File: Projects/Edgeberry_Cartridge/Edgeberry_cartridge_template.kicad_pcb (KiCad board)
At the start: 2 copper layers, 49.8 x 63.2 mm, 2 parts

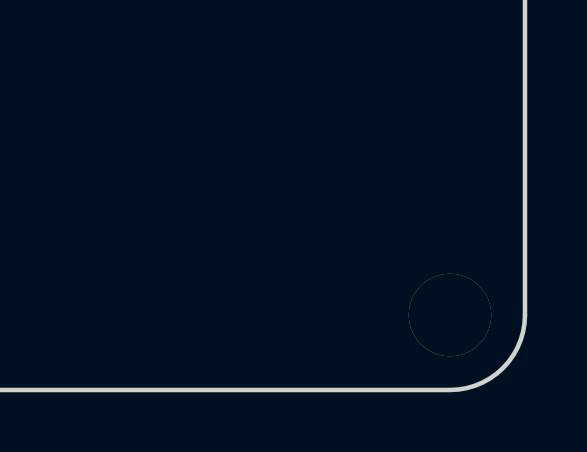
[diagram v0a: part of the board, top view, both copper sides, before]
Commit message: Update - Edgeberry Template improve documentation, make mounting hole manufacturable, include template for faceplate.
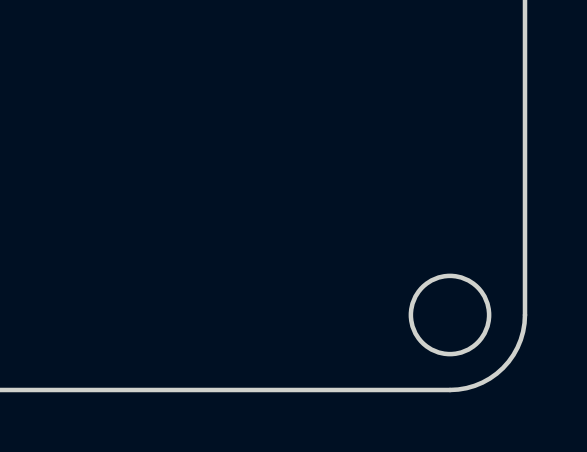
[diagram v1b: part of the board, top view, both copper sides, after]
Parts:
- removed REF**: Hole_M2.5_small, emcosys:Hole_M2.5_small
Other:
- outline, holes or cut-outs redrawn
- board text added: "To fit the standard Edgeberry enclosure, components on the top side should not exceed a height of 15mm, and on the bottom side 1.5mm. A margin of at least 2mm on the left and right side of the board must be left clear of components to fit the enclosure The backplate of the enclosure has a thickness of about 2mm. you can put components, for example connectors, a bit over the edge of the board. Fin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"
- board text removed: "To fit the standard Edgeberry enclosure, components on the top side should exceed a height of 15mm, and on the bottom side 1.5mm. A margin of at least 2mm on the left and right side of the board must be left clear of components to fit the enclosure The backplate of the enclosure has a thickness of about 2mm. you can put components, for example connectors, a bit over the edge of the board. Find mo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"
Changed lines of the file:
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@@
 	(net 31 "unconnected-(H1-UART_Rx-Pad26)")
 	(net 32 "unconnected-(H1-3V3_Power-Pad15)")
-	(footprint "emcosys:Hole_M2.5_small"
-		(layer "F.Cu")
-		(at 172.5 132.5)
-		(property "Reference" "REF**"
-			(at 0 -2.54 0)
-			(layer "F.SilkS")
-			(hide yes)
-			(effects
-				(font
-					(size 1 1)
-					(thickness 0.15)
-				)
-			)
-		)
-		(property "Value" "Hole_M2.5_small"
-			(at 0 -2.54 0)
-			(layer "F.Fab")
-			(hide yes)
-			(effects
-				(font
-					(size 1 1)
-					(thickness 0.15)
-				)
-			)
-		)
-		(property "Footprint" "emcosys:Hole_M2.5_small"
-			(at 0 0 0)
-			(unlocked yes)
-			(layer "F.Fab")
-			(hide yes)
-			(effects
-				(font
-					(size 1.27 1.27)
-				)
-			)
-		)
-		(property "Datasheet" ""
-			(at 0 0 0)
-			(unlocked yes)
-			(layer "F.Fab")
-			(hide yes)
-			(effects
-				(font
-					(size 1.27 1.27)
-				)
-			)
-		)
-		(property "Description" ""
-			(at 0 0 0)
-			(unlocked yes)
-			(layer "F.Fab")
-			(hide yes)
-			(effects
-				(font
-					(size 1.27 1.27)
-				)
-			)
-		)
-		(attr through_hole)
-		(pad "1" thru_hole circle
-			(at 0 0)
-			(size 2.75 2.75)
-			(drill 2.75)
-			(layers "*.Cu" "*.Mask")
-			(remove_unused_layers no)
-		)
-	)
 	(footprint "Connector_PinHeader_2.54mm:PinHeader_2x16_P2.54mm_Horizontal"
 		(locked yes)
@@
 				(font
 					(size 1.27 1.27)
+					(thickness 0.15)
 				)
 			)
@@
 				(font
 					(size 1.27 1.27)
+					(thickness 0.15)
 				)
 			)
@@
 				(font
 					(size 1.27 1.27)
+					(thickness 0.15)
 				)
 			)
@@
 				(font
 					(size 1.27 1.27)
+					(thickness 0.15)
 				)
 			)
@@
 			)
 		)
+		(model "${KIPRJMOD}/faceplate/Edgeberry_Hardware_Cartridge_faceplate.step"
+			(offset
+				(xyz -43.5 -31.5 4.5)
+			)
+			(scale
+				(xyz 1 1 1)
+			)
+			(rotate
+				(xyz -90 0 90)
+			)
+		)
 	)
 	(gr_line
@@
 		(layer "Dwgs.User")
 	)
+	(gr_line
+		(start 177.2 43)
+		(end 175.2 43)
+		(stroke
+			(width 0.1)
+			(type default)
+		)
+		(layer "Dwgs.User")
+	)
 	(gr_poly
 		(pts
@@
 		(layer "Dwgs.User")
 	)
+	(gr_line
+		(start 175.2 43)
+		(end 175.2 138)
+		(stroke
+			(width 0.1)
+			(type default)
+		)
+		(layer "Dwgs.User")
+	)
 	(gr_poly
 		(pts
@@
 	)
 	(gr_line
+		(start 175.2 138)
+		(end 177.2 138)
+		(stroke
+			(width 0.1)
+			(type default)
+		)
+		(layer "Dwgs.User")
+	)
+	(gr_line
+		(start 177.2 138)
+		(end 177.2 43)
+		(stroke
+			(width 0.1)
+			(type default)
+		)
+		(layer "Dwgs.User")
+	)
+	(gr_line
 		(start 177 71.8)
 		(end 177 135)
@@
 		(layer "Edge.Cuts")
 	)
+	(gr_circle
+		(center 172.5 132.5)
+		(end 171.8 131.4)
+		(stroke
+			(width 0.15)
+			(type default)
+		)
+		(fill none)
+		(layer "Edge.Cuts")
+	)
 	(gr_line
 		(start 175 132.5)
@@
 		)
 	)
-	(gr_text "To fit the standard Edgeberry enclosure,\ncomponents on the top side should exceed\na height of 15mm, and on the bottom side\n1.5mm.\n\nA margin of at least 2mm on the left and\nright side of the board must be left clear\nof components to fit the enclosure\n\nThe backplate of the enclosure has a\nthickness of about 2mm. you can put\ncomponents, for example connectors, a\nbit over the edge of the board.\n\nFind more info on the Edgeberry project\non GitHub:\nhttps://github.com/SpuQ/EdgeBerry"
+	(gr_text "To fit the standard Edgeberry enclosure,\ncomponents on the top side should not\nexceed a height of 15mm, and on the \nbottom side 1.5mm.\n\nA margin of at least 2mm on the left and\nright side of the board must be left clear\nof components to fit the enclosure\n\nThe backplate of the enclosure has a\nthickness of about 2mm. you can put\ncomponents, for example connectors, a\nbit over the edge of the board.\n\nFind more info on the Edgeberry project\non GitHub:\nhttps://github.com/Edgeberry"
 		(at 191.075 110.625 0)
 		(layer "Dwgs.User")
@@
 		)
 		(height -3.7)
-		(gr_text "6,6 mm"
+		(gr_text "6.6 mm"
 			(at 128.575 127.925 0)
 			(layer "Dwgs.User")
@@
 		)
 		(height -2.85)
-		(gr_text "13,0 mm"
+		(gr_text "13.0 mm"
 			(at 133.5 128.475 90)
 			(layer "Dwgs.User")
@@
 			(extension_offset 0) keep_text_aligned)
 	)
+	(zone
+		(net 0)
+		(net_name "")
+		(layer "Dwgs.User")
+		(hatch edge 0.5)
+		(connect_pads
+			(clearance 0.2)
+		)
+		(min_thickness 0.25)
+		(filled_areas_thickness no)
+		(fill yes
+			(thermal_gap 0.5)
+			(thermal_bridge_width 0.5)
+		)
+		(polygon
+			(pts
+				(xy 175.2 138) (xy 177.2 138) (xy 177.2 43) (xy 175.2 43)
+			)
+		)
+	)
 )
